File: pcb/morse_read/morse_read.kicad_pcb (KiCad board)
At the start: 2 copper layers, 100 x 100 mm, 62 parts, among them J1 Screw_Terminal_01x04, J2 Conn_01x04_Female, J3 Conn_01x02_Female, J4 Conn_01x02_Female, J5 Conn_01x02_Female, J6 Conn_01x02_Female, J7 Conn_01x02_Female, J8 Conn_01x02_Female, Q1 AO3400A, Q2 AO3400A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

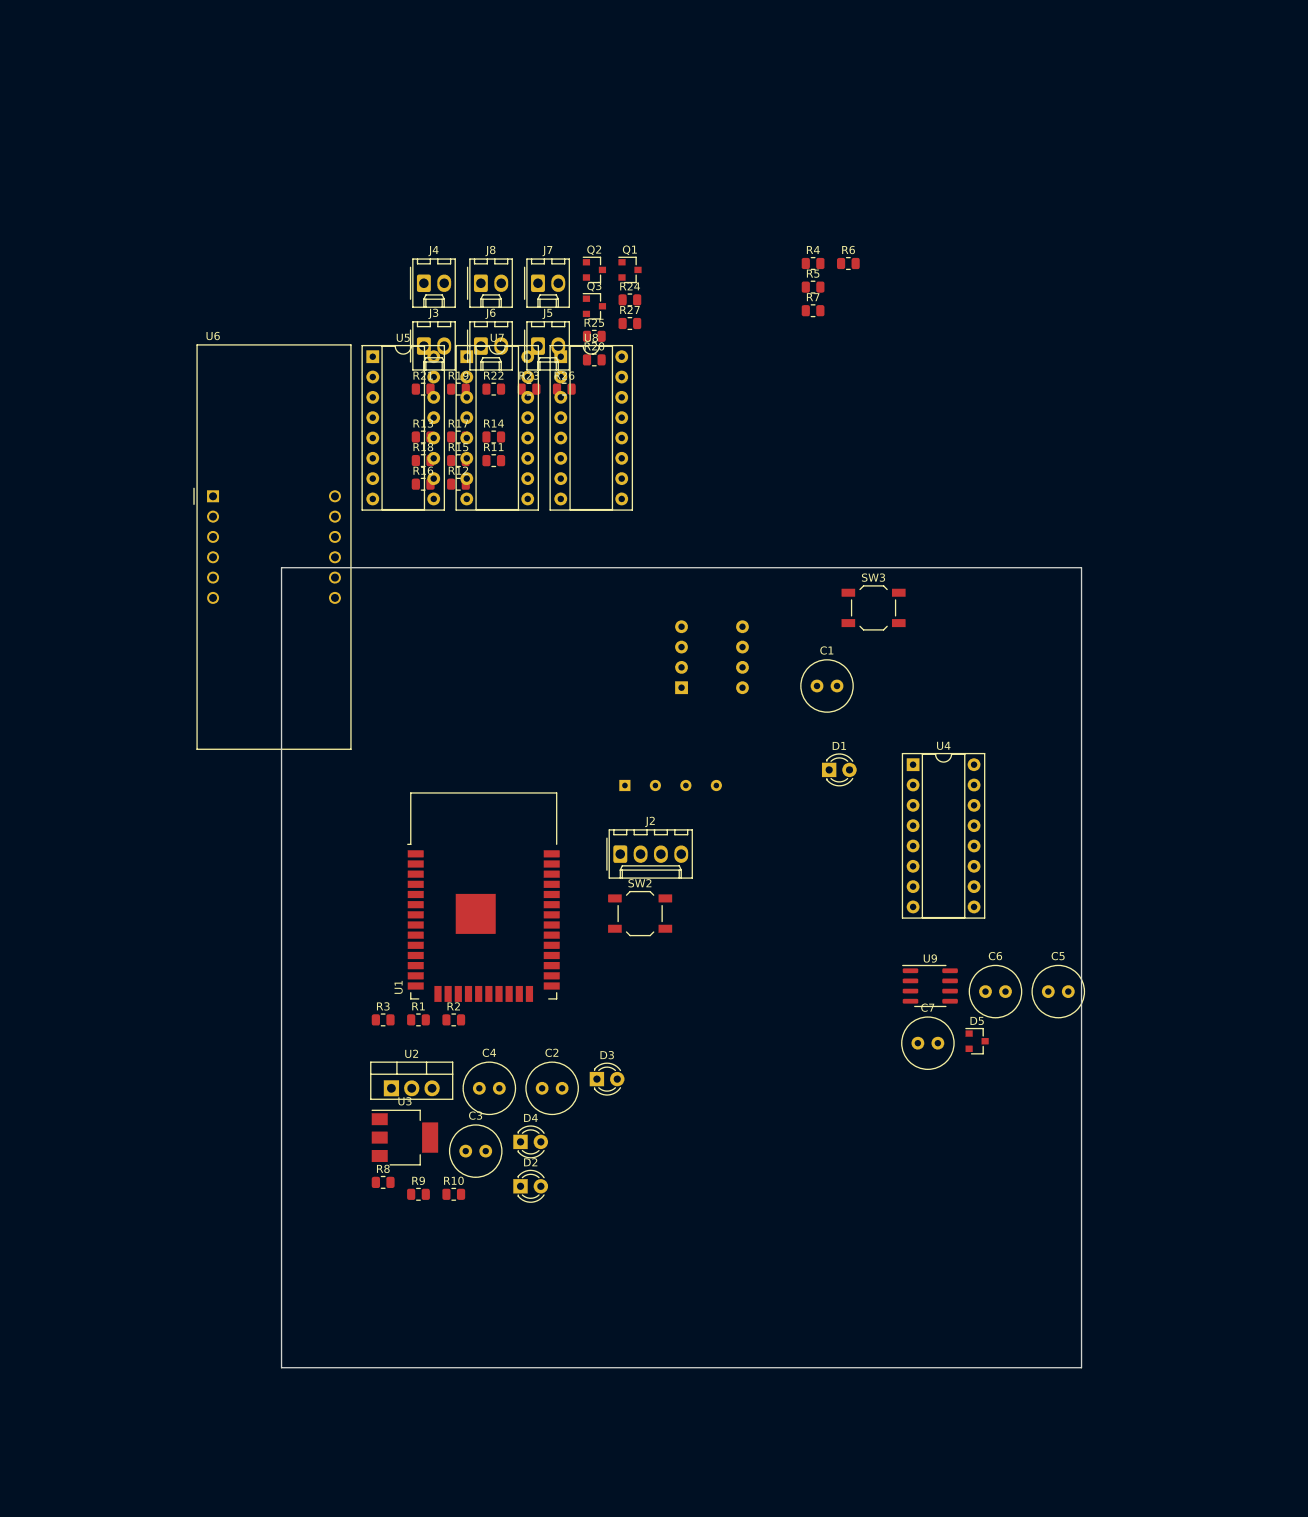
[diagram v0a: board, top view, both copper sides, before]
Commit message: PCB completed exept Multiplexer and Frontbuttons & LED scematics updated
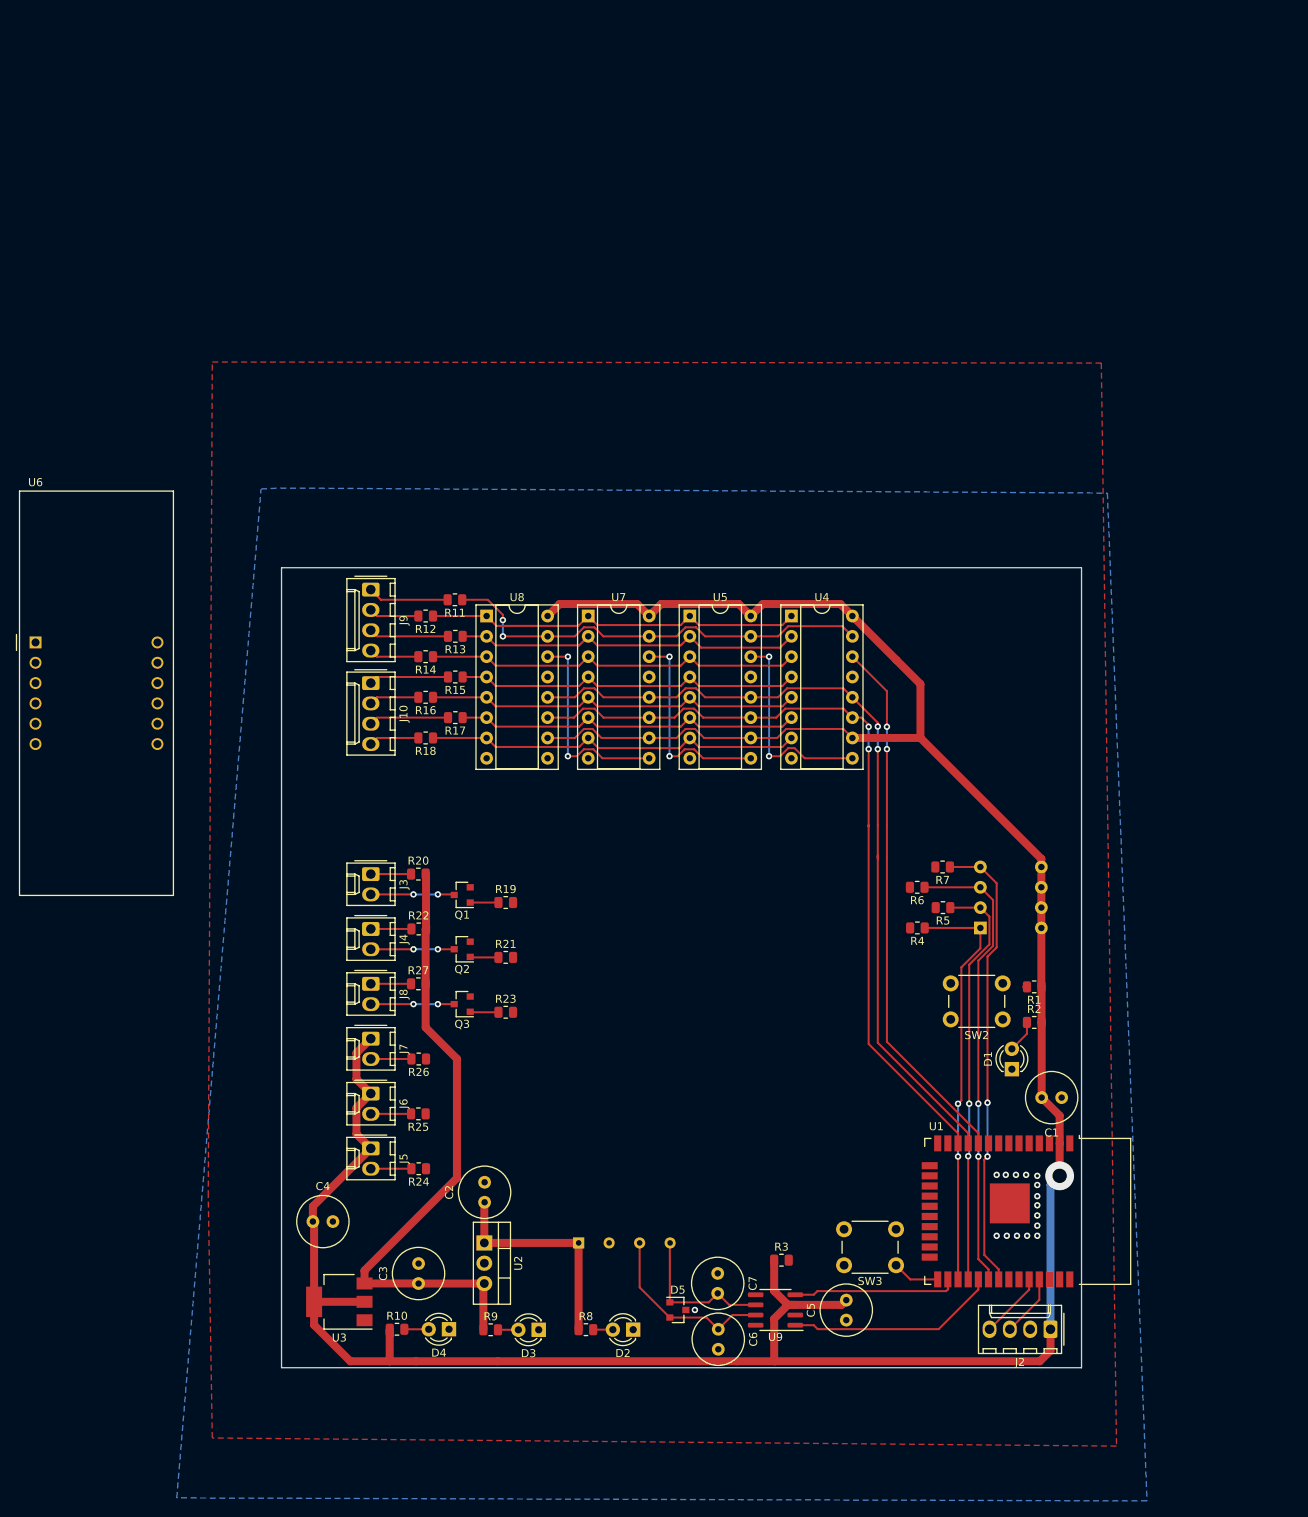
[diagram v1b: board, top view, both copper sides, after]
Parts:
- added J10: Conn_01x04_Female, Connector_Molex:Molex_KK-254_AE-6410-04A_1x04_P2.54mm_Vertical, F.Cu at (121.2, 74.4)
- added J9: Conn_01x04_Female, Connector_Molex:Molex_KK-254_AE-6410-04A_1x04_P2.54mm_Vertical, F.Cu at (121.2, 62.7)
- SW2, SW3: footprint Button_Switch_SMD:SW_SPST_TL3342 -> Button_Switch_THT:SW_PUSH_6mm
- moved R24 111.8 mm to (127.2, 135.1), turned to 180 degrees
- moved J5 102.4 mm to (121.2, 132.6), turned to 270 degrees
- moved R25 99.7 mm to (127.1, 128.3), turned to 180 degrees
- moved J7 96.7 mm to (121.2, 118.9), turned to 270 degrees
- moved J6 94.4 mm to (121.2, 125.7), turned to 270 degrees
- moved Q3 88.8 mm to (132.6, 114.6), turned to 180 degrees
- moved J8 88.6 mm to (121.2, 112.0), turned to 270 degrees
- moved R27 86.7 mm to (127.1, 112.0)
- moved Q2 86.5 mm to (132.6, 107.7), turned to 180 degrees
- moved R26 85.7 mm to (127.2, 121.4), turned to 180 degrees
- moved R4 84.1 mm to (189.5, 105.0), turned to 180 degrees
- moved SW3 82.2 mm to (186.8, 147.2), turned to 180 degrees
- moved J4 81.0 mm to (121.2, 105.2), turned to 270 degrees
- moved Q1 80.9 mm to (132.6, 100.9), turned to 180 degrees
- moved J2 80.1 mm to (206.1, 155.2), turned to 180 degrees
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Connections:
- R11 pad 2: Net-(R11-Pad2) -> Net-(J9-Pad1)
- R12 pad 2: Net-(R12-Pad2) -> Net-(J9-Pad2)
- R13 pad 2: Net-(R13-Pad2) -> Net-(J9-Pad3)
- R14 pad 2: Net-(R14-Pad2) -> Net-(J9-Pad4)
- R15 pad 2: Net-(R15-Pad2) -> Net-(J10-Pad1)
- R16 pad 2: Net-(R16-Pad2) -> Net-(J10-Pad2)
- R17 pad 2: Net-(R17-Pad2) -> Net-(J10-Pad3)
- R18 pad 2: Net-(R18-Pad2) -> Net-(J10-Pad4)
- U1 pad 10: /SRCLK -> /SER
- U1 pad 12: /SER -> /SRCLK
- U6 pad 1: Net-(R15-Pad2) -> Net-(U6-Pad1)
- U6 pad 10: Net-(R16-Pad2) -> Net-(U6-Pad10)
- U6 pad 11: Net-(R11-Pad2) -> Net-(U6-Pad11)
- U6 pad 2: Net-(R14-Pad2) -> Net-(U6-Pad2)
- U6 pad 3: Net-(R18-Pad2) -> Net-(U6-Pad3)
- U6 pad 4: Net-(R13-Pad2) -> Net-(U6-Pad4)
- U6 pad 5: Net-(R17-Pad2) -> Net-(U6-Pad5)
- U6 pad 7: Net-(R12-Pad2) -> Net-(U6-Pad7)
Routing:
- net +3V3: track 0.00 -> 364.5 mm, vias 0 -> 1
- net /RCLK: track 0.00 -> 103.3 mm, vias 0 -> 2
- net /SRCLK: track 0.00 -> 100.5 mm, vias 0 -> 2
- net +5V: track 0.00 -> 78.6 mm
- net /SER: track 0.00 -> 67.4 mm, vias 0 -> 2
- net /DIP_3: track 0.00 -> 57.9 mm, vias 0 -> 2
- net /DIP_4: track 0.00 -> 57.6 mm, vias 0 -> 2
- net /Shiftregister/QA: track 0.00 -> 55.2 mm, vias 0 -> 2
- net /DIP_2: track 0.00 -> 53.5 mm, vias 0 -> 2
- net /DIP_1: track 0.00 -> 52.4 mm, vias 0 -> 2
- net /Shiftregister/QB: track 0.00 -> 47.8 mm
- net /Shiftregister/QH: track 0.00 -> 47.7 mm
- net /Shiftregister/QF: track 0.00 -> 47.6 mm
- net /Shiftregister/QD: track 0.00 -> 47.6 mm
- net /Shiftregister/QC: track 0.00 -> 44.1 mm
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- added copper zone on B.Cu, net GND
- added copper zone on F.Cu, net GND
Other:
- net class 1mm added: clearance 0.2, trace_width 1, via_dia 3.6, via_drill 1.8
- net class Default: trace_width 0.25 -> 0.254
- rule trace_min: 0.2 -> 0.254
- board text added: "hier platz für multiplexer"

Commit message: PCB update  new size 97*97 mm
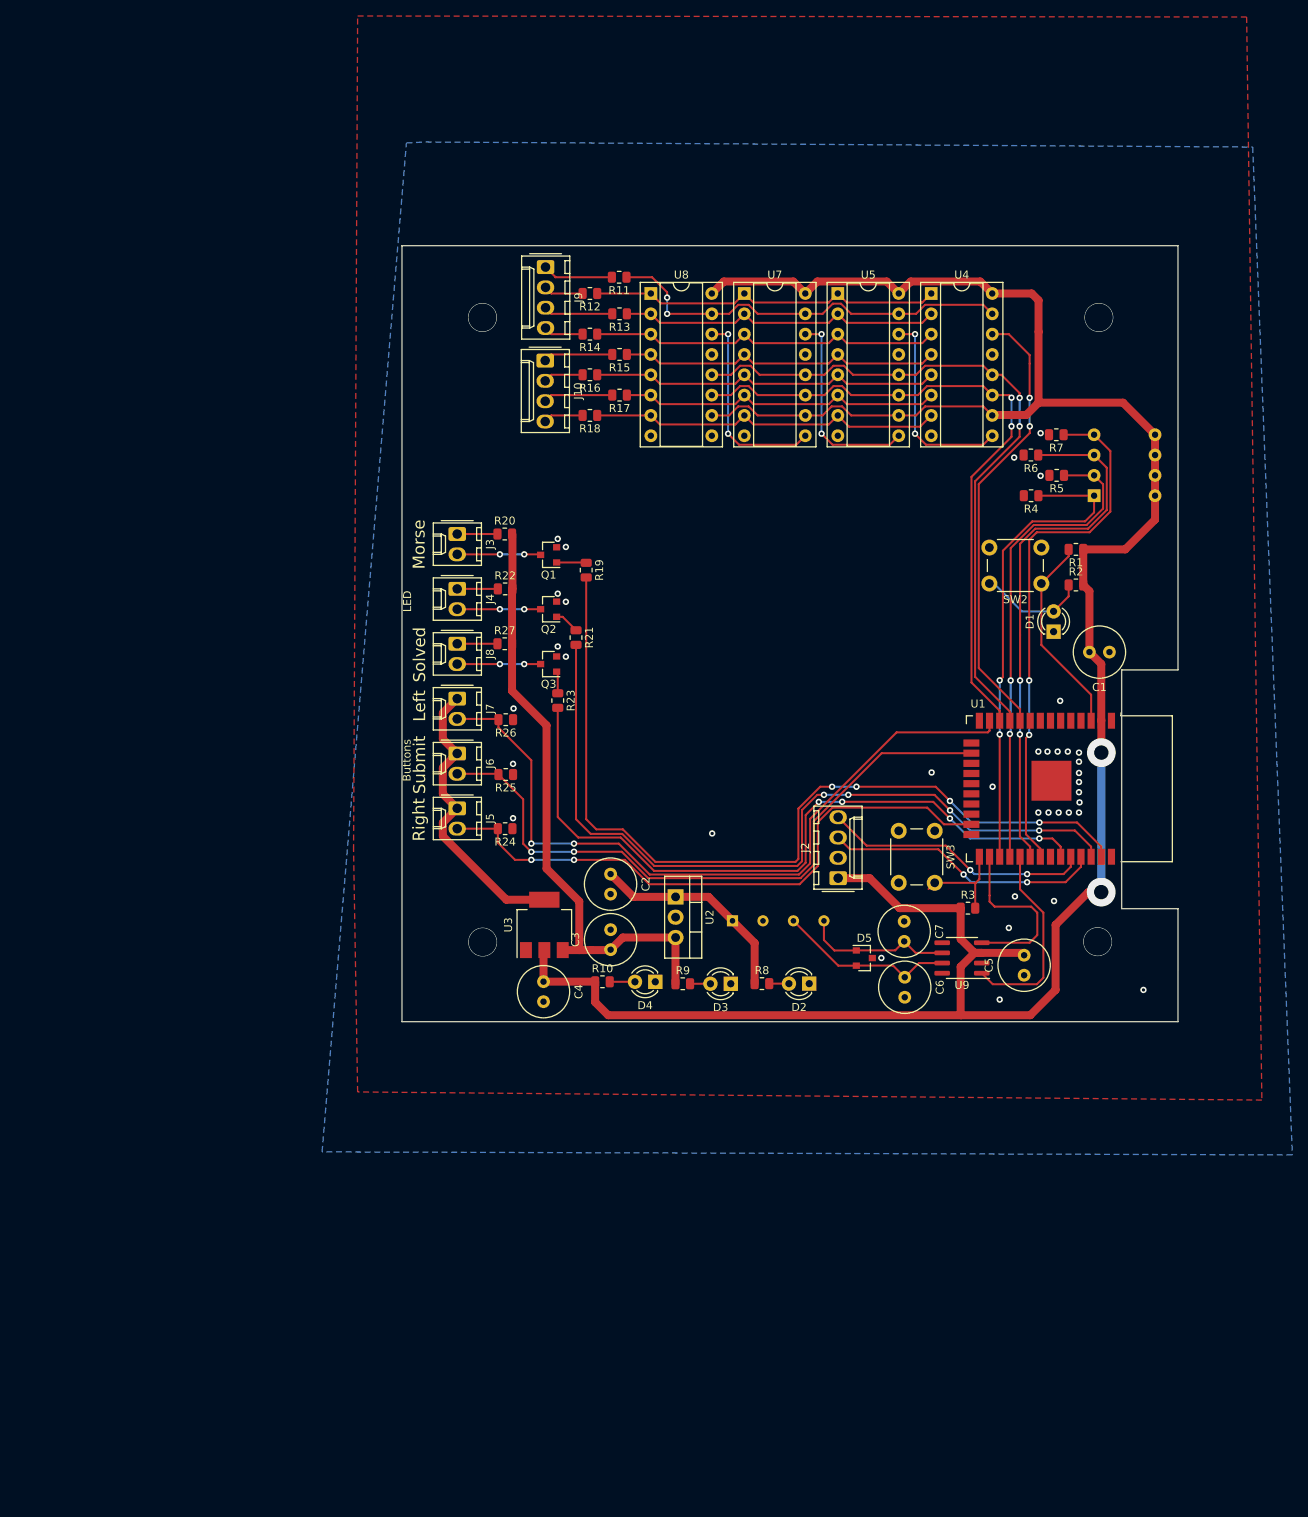
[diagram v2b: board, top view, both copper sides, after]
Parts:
- removed U6: CC56-12SURKWA, Display_7Segment:CA56-12SURKWA
- moved J2 62.3 mm to (179.6, 98.8), turned to 90 degrees
- moved C1 56.0 mm to (213.5, 70.5)
- moved R5 55.9 mm to (206.9, 48.5)
- moved R6 55.9 mm to (203.7, 45.9)
- moved R7 55.9 mm to (206.8, 43.4)
- moved R4 55.9 mm to (203.7, 51.0)
- moved SW1 55.9 mm to (211.6, 51.0)
- moved D1 54.9 mm to (206.5, 68.0)
- moved R2 54.9 mm to (209.3, 62.2)
- moved R1 54.9 mm to (209.3, 57.7)
- moved SW2 54.7 mm to (205.0, 62.0)
- moved SW3 54.5 mm to (191.6, 92.9), turned to 270 degrees
- moved U3 53.6 mm to (142.8, 104.6), turned to 90 degrees
- moved U1 53.1 mm to (205.5, 87.6)
- moved D4 50.5 mm to (156.7, 111.8)
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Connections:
- J5 pad 2: /front/Right_Button -> /Right_Button
- J6 pad 2: /front/Submit_Button -> /Submit_Button
- J7 pad 2: /front/Left_Button -> /Left_Button
- R19 pad 2: /front/Morse_LED -> /Morse_LED
- R21 pad 2: /front/Strike_LED -> /Strike_LED
- R23 pad 2: /front/Solved_LED -> /Solved_LED
- R24 pad 2: /front/Right_Button -> /Right_Button
- R25 pad 2: /front/Submit_Button -> /Submit_Button
- R26 pad 2: /front/Left_Button -> /Left_Button
- SW2 pad 1: Net-(R1-Pad2) -> Net-(D1-Pad2)
- U1 pad 13: Net-(U1-Pad13) -> /Left_Button
- U1 pad 16: Net-(U1-Pad16) -> /Submit_Button
- U1 pad 23: Net-(U1-Pad23) -> /Right_Button
- U1 pad 33: Net-(U1-Pad33) -> /Solved_LED
- U1 pad 36: Net-(U1-Pad36) -> /Strike_LED
- U1 pad 37: Net-(U1-Pad37) -> /Morse_LED
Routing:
- net /Morse_LED: track 0.00 -> 109.0 mm, vias 0 -> 4
- net /Strike_LED: track 0.00 -> 100.0 mm, vias 0 -> 4
- net /Left_Button: track 0.00 -> 93.1 mm, vias 0 -> 2
- net /Solved_LED: track 0.00 -> 89.9 mm, vias 0 -> 4
- net /Submit_Button: track 0.00 -> 82.5 mm, vias 0 -> 2
- net /Right_Button: track 0.00 -> 76.2 mm, vias 0 -> 2
- net /TX: track 7.76 -> 34.7 mm, vias 0 -> 2
- net /RX: track 8.28 -> 33.7 mm, vias 0 -> 2
- net Net-(R1-Pad2): track 0.48 -> 25.4 mm
- net +3V3: track 364.5 -> 348.0 mm, vias 1 -> 2
- net /RCLK: track 103.3 -> 87.4 mm
- net /SRCLK: track 100.5 -> 84.7 mm
- net /SER: track 67.4 -> 56.3 mm
- net /DIP_4: track 57.6 -> 67.6 mm
- net /DIP_3: track 57.9 -> 67.6 mm
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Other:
- board size 100 x 100 mm -> 97 x 97 mm
- board text added: "Buttons"
- board text added: "LED"
- board text added: "Left"
- board text added: "Morse"
- board text added: "Right"
- board text added: "Solved"
- board text added: "Strike"
- board text added: "Submit"
